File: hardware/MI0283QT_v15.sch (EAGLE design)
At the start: 38 parts, among them IC1 ADS7846PW, IC2 74244PW, IC3 VREG-TS9011-3V3, J1 MA08-2, J2 MA08-1, T1 N-Chn, X1 PASSER-07, X2 PASSER-07, X3 PASSER-07, X4 PASSER-07

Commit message: update schematics
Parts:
- renumbered BUSY-RS to RS-BUSY
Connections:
- net N$6 renamed BUSY_RS
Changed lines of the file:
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@@
 <part name="C7" library="we-rcl" deviceset="CAPACITOR" device="-0402" value="100n"/>
 <part name="C9" library="we-rcl" deviceset="CAPACITOR" device="-0402" value="100n"/>
-<part name="BUSY-RS" library="we-rcl" deviceset="JUMPER3" device="-0603" value="JUMPER3-0603"/>
+<part name="RS-BUSY" library="we-rcl" deviceset="JUMPER3" device="-0603" value="JUMPER3-0603"/>
 <part name="VCC-3V3" library="we-rcl" deviceset="JUMPER2" device="-0603-NC" value="JUMPER2-0603-NC"/>
 <part name="T1" library="we-transistor" deviceset="MOSFET-N" device="-SOT23" value="N-Chn"/>
@@
 </instance>
 <instance part="C9" gate="C" x="97.79" y="109.22" rot="R90"/>
-<instance part="BUSY-RS" gate="J" x="232.41" y="48.26"/>
+<instance part="RS-BUSY" gate="J" x="232.41" y="48.26"/>
 <instance part="VCC-3V3" gate="J" x="116.84" y="25.4"/>
 <instance part="T1" gate="T" x="85.09" y="119.38" smashed="yes" rot="MR270">
@@
 <wire x1="232.41" y1="55.88" x2="232.41" y2="53.34" width="0.1524" layer="91"/>
 <label x="232.41" y="55.88" size="1.27" layer="95" rot="R90" xref="yes"/>
-<pinref part="BUSY-RS" gate="J" pin="1"/>
+<pinref part="RS-BUSY" gate="J" pin="1"/>
 </segment>
 </net>
@@
 <wire x1="232.41" y1="40.64" x2="232.41" y2="43.18" width="0.1524" layer="91"/>
 <label x="232.41" y="40.64" size="1.27" layer="95" rot="R270" xref="yes"/>
-<pinref part="BUSY-RS" gate="J" pin="3"/>
+<pinref part="RS-BUSY" gate="J" pin="3"/>
 </segment>
 <segment>
@@
 </segment>
 </net>
-<net name="N$6" class="0">
+<net name="BUSY_RS" class="0">
 <segment>
 <wire x1="205.74" y1="48.26" x2="227.33" y2="48.26" width="0.1524" layer="91"/>
-<pinref part="BUSY-RS" gate="J" pin="2"/>
+<pinref part="RS-BUSY" gate="J" pin="2"/>
 <pinref part="J1" gate="J" pin="12"/>
 </segment>

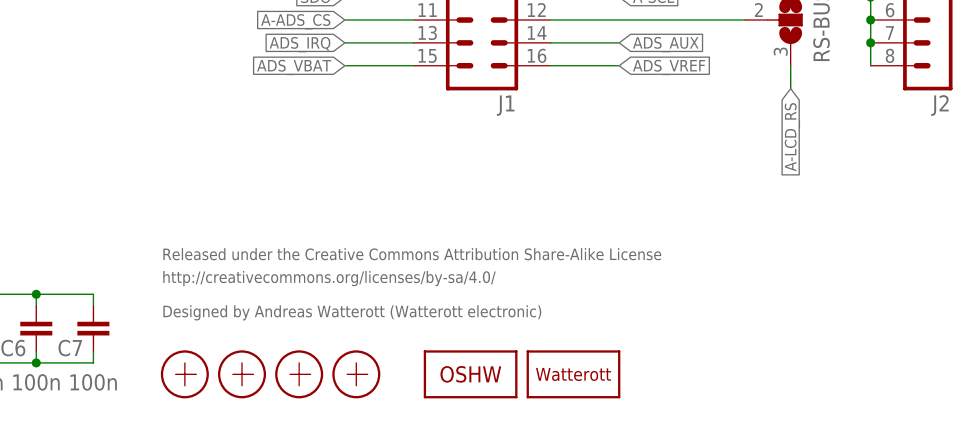
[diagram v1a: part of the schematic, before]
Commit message: updated schematics
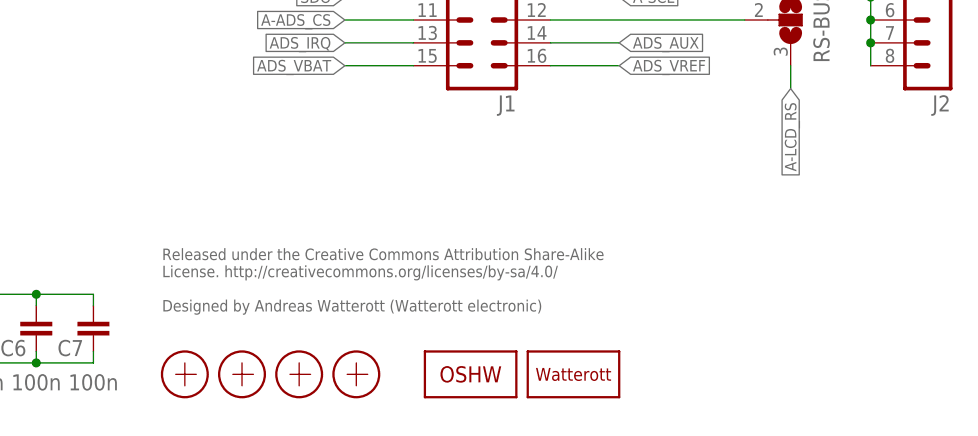
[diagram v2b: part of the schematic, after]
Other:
- note added: "Released under the Creative Commons Attribution Share-Alike License. http://creativecommons.org/licenses/by-sa/4.0/ Designed by Andreas Watterott (Watterott electronic)"
- note removed: "Designed by Andreas Watterott (Watterott electronic)"
- note removed: "Released under the Creative Commons Attribution Share-Alike License"
- note removed: "http://creativecommons.org/licenses/by-sa/4.0/"
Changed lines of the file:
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@@
 <setting verticaltext="up"/>
 </settings>
-<grid distance="0.1" unitdist="inch" unit="inch" style="lines" multiple="1" display="no" altdistance="0.01" altunitdist="inch" altunit="inch"/>
+<grid distance="0.05" unitdist="inch" unit="inch" style="lines" multiple="1" display="yes" altdistance="0.025" altunitdist="inch" altunit="inch"/>
 <layers>
 <layer number="1" name="Top" color="4" fill="1" visible="no" active="no"/>
@@
 <layer number="51" name="tDocu" color="7" fill="1" visible="no" active="no"/>
 <layer number="52" name="bDocu" color="7" fill="1" visible="no" active="no"/>
-<layer number="53" name="tCopper" color="7" fill="11" visible="no" active="no"/>
-<layer number="54" name="bCopper" color="7" fill="1" visible="no" active="no"/>
-<layer number="56" name="wert" color="7" fill="1" visible="no" active="no"/>
-<layer number="57" name="tCAD" color="7" fill="1" visible="no" active="no"/>
-<layer number="60" name="Board" color="7" fill="1" visible="no" active="no"/>
 <layer number="90" name="Modules" color="5" fill="1" visible="yes" active="yes"/>
 <layer number="91" name="Nets" color="2" fill="1" visible="yes" active="yes"/>
@@
 <text x="45.085" y="146.685" size="1.778" layer="95">1</text>
 <text x="45.085" y="139.065" size="1.778" layer="95">1</text>
-<text x="162.56" y="21.59" size="1.27" layer="95">Released under the Creative Commons Attribution Share-Alike License</text>
-<text x="162.56" y="19.05" size="1.27" layer="95">http://creativecommons.org/licenses/by-sa/4.0/</text>
-<text x="162.56" y="15.24" size="1.27" layer="95">Designed by Andreas Watterott (Watterott electronic)</text>
+<text x="162.56" y="22.86" size="1.27" layer="95" align="top-left">Released under the Creative Commons Attribution Share-Alike
+License. http://creativecommons.org/licenses/by-sa/4.0/
+Designed by Andreas Watterott (Watterott electronic)</text>
 <text x="26.67" y="166.37" size="3.81" layer="250">Display with Touch-Panel</text>
 <wire x1="105.41" y1="65.024" x2="105.41" y2="67.183" width="0.8128" layer="94"/>
@@
 </schematic>
 </drawing>
+<compatibility>
+<note version="6.3" minversion="6.2.2" severity="warning">
+Since Version 6.2.2 text objects can contain more than one line,
+which will not be processed correctly with this version.
+</note>
+</compatibility>
 </eagle>
